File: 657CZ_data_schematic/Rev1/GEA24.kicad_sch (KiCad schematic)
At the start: 4 parts, among them J241 DE9_Socket, J242 DB25_Socket, J244 DB50_Socket

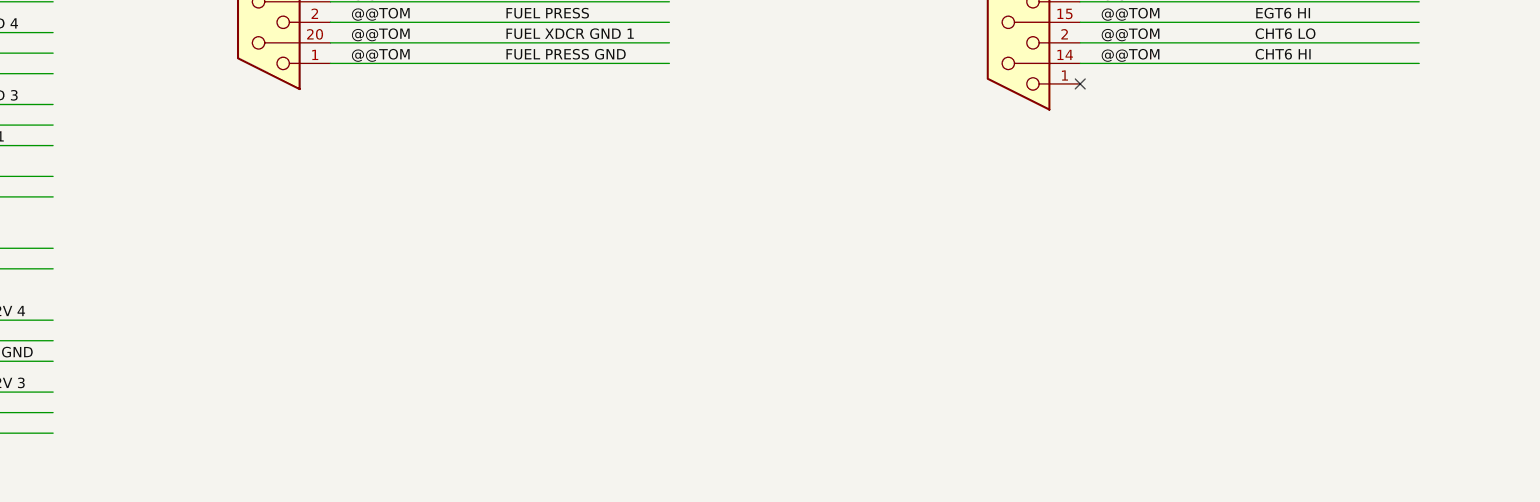
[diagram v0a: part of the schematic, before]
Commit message: added data connections after AvClassics wiring. completed LRUs GMU, GDU, GSU, GAD, GNC, GTX, GTR  Not completed GMA, GEA and autopilot LRUs
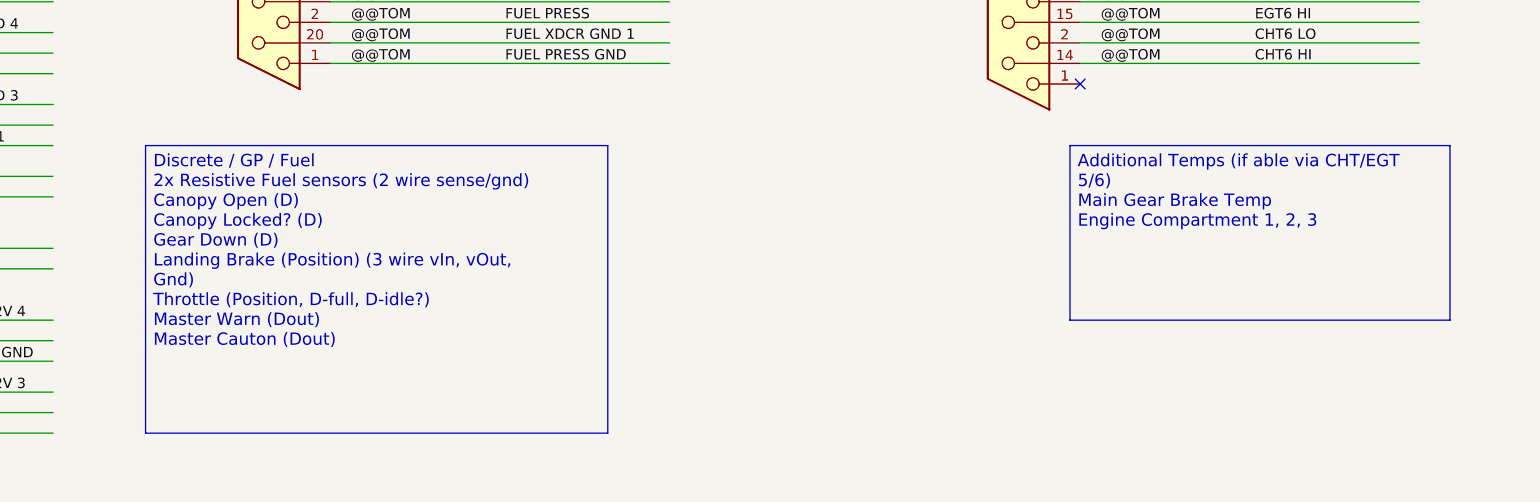
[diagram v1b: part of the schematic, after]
